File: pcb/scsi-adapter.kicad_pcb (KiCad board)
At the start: 4 copper layers, 120 x 90 mm, 406 parts, among them J101 Bench 5V, J201 TERMPWR jumper, J301 IDC50 box header, J302 HD50 female R/A, J303 2x17 box header, J401 TC2030-IDC, J501 TF PUSH, J601 USB-C (HRO TYPE-C-31-M-12), Q1001 FDV301N, Q1101 FDV301N, Q1201 FDV301N, Q1301 FDV301N, Q1401 FDV301N, Q1501 FDV301N, Q1601 FDV301N, Q1701 FDV301N, Q1801 FDV301N, Q1901 FDV301N, Q2001 FDV301N, Q201 2N7002, Q2101 FDV301N, Q2301 FDV301N, Q901 FDV301N, SW301 DIP 2-pos, SW401 BOOTSEL, SW402 RUN, U1001 74LVC1G17GW, U101 TPS259470ARPWR, U102 TPS2116DRLR, U103 TPS73701DCQR, U104 TPS73701DCQR, U1101 74LVC1G17GW, U1201 74LVC1G17GW, U1301 74LVC1G17GW, U1401 74LVC1G17GW, U1501 74LVC1G17GW, U1601 74LVC1G17GW, U1701 74LVC1G17GW, U1801 74LVC1G17GW, U1901 74LVC1G17GW, U2001 74LVC1G17GW, U201 TPS259470ARPWR, U202 LM393DR2G, U203 CJ431, U2101 74LVC1G17GW, U2201 74LVC1G17GW, U2301 74LVC1G17GW, U2401 74LVC1G17GW, U2501 74LVC1G17GW, U2601 74LVC1G17GW, U301 SN74LVTH245APWR, U302 SN74LVTH245APWR, U303 SN74LVTH245APWR, U401 RP2350B, U402 W25Q128JVSIQ, U403 APS6404L-3SQR-SN, U501 TCA9555PWR, U601 CH334P, U701 FT232HL, U702 93LC56BT-I/OT, U901 74LVC1G17GW, Y401 12MHz ABM8-272-T3, Y601 12MHz ABM8-272-T3, Y701 12MHz ABM8-272-T3

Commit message: more manual iteration
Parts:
- moved C108 0.41 mm to (105.2, 87.0)
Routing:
- net GND: track 291.4 -> 297.9 mm, vias 193 -> 195
- net /BENCH_5V: track 23.3 -> 24.6 mm
- net /scsi/~{DB0}: track 164.9 -> 163.8 mm
- net /scsi/~{DB2}: track 166.5 -> 165.4 mm
- net /scsi/~{DB1}: track 165.3 -> 164.1 mm
- net /scsi/~{MSG}: track 86.4 -> 85.3 mm
- net /scsi/~{BSY}: track 101.4 -> 100.3 mm
- net /scsi/~{SEL}: track 89.7 -> 88.6 mm
- net /scsi/~{RST}: track 86.0 -> 84.9 mm
- net /scsi/~{IO}: track 74.1 -> 72.9 mm
- net /scsi/~{DBP}: track 144.2 -> 143.1 mm
- net /scsi/~{DB6}: track 143.9 -> 142.7 mm
- net /scsi/~{DB5}: track 155.3 -> 154.1 mm
- net /scsi/~{DB4}: track 154.4 -> 153.3 mm
- net /scsi/~{DB3}: track 154.5 -> 153.4 mm
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
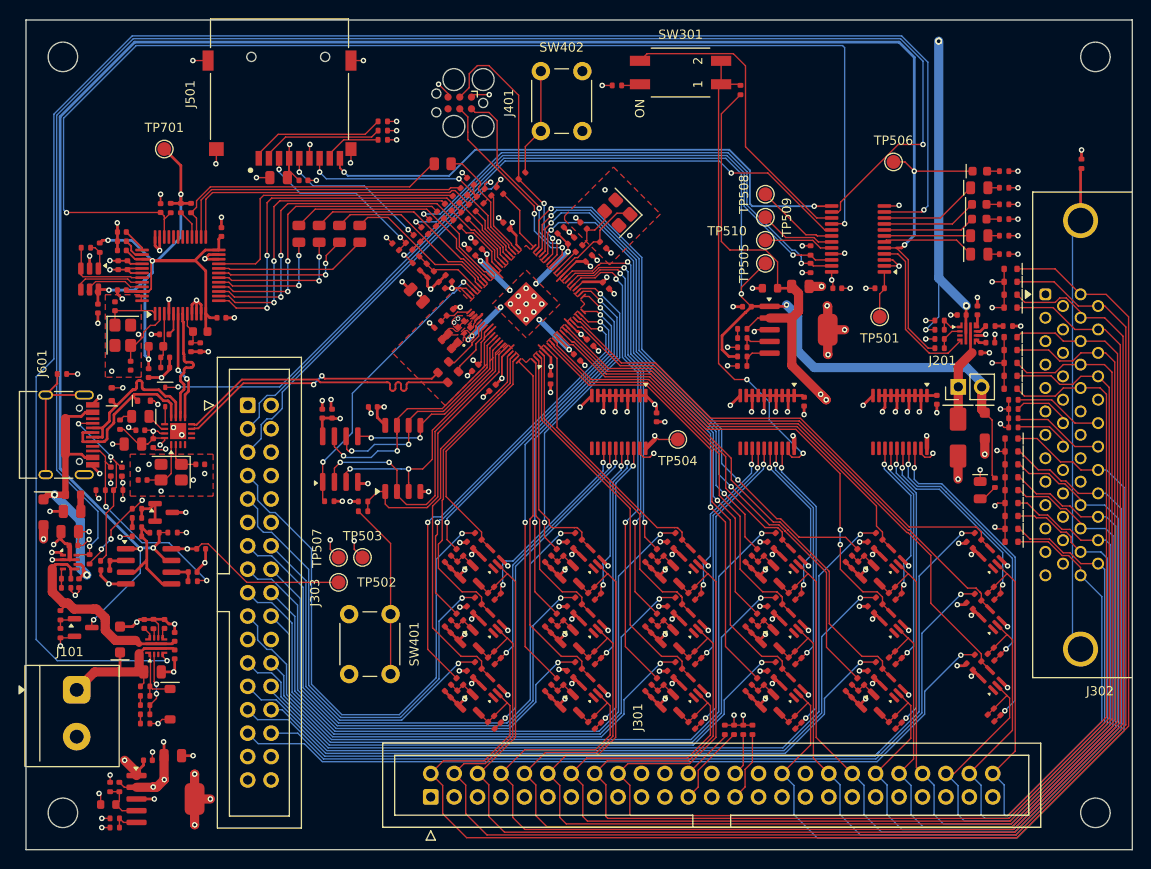
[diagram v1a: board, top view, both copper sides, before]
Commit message: thermal pours for LDOs
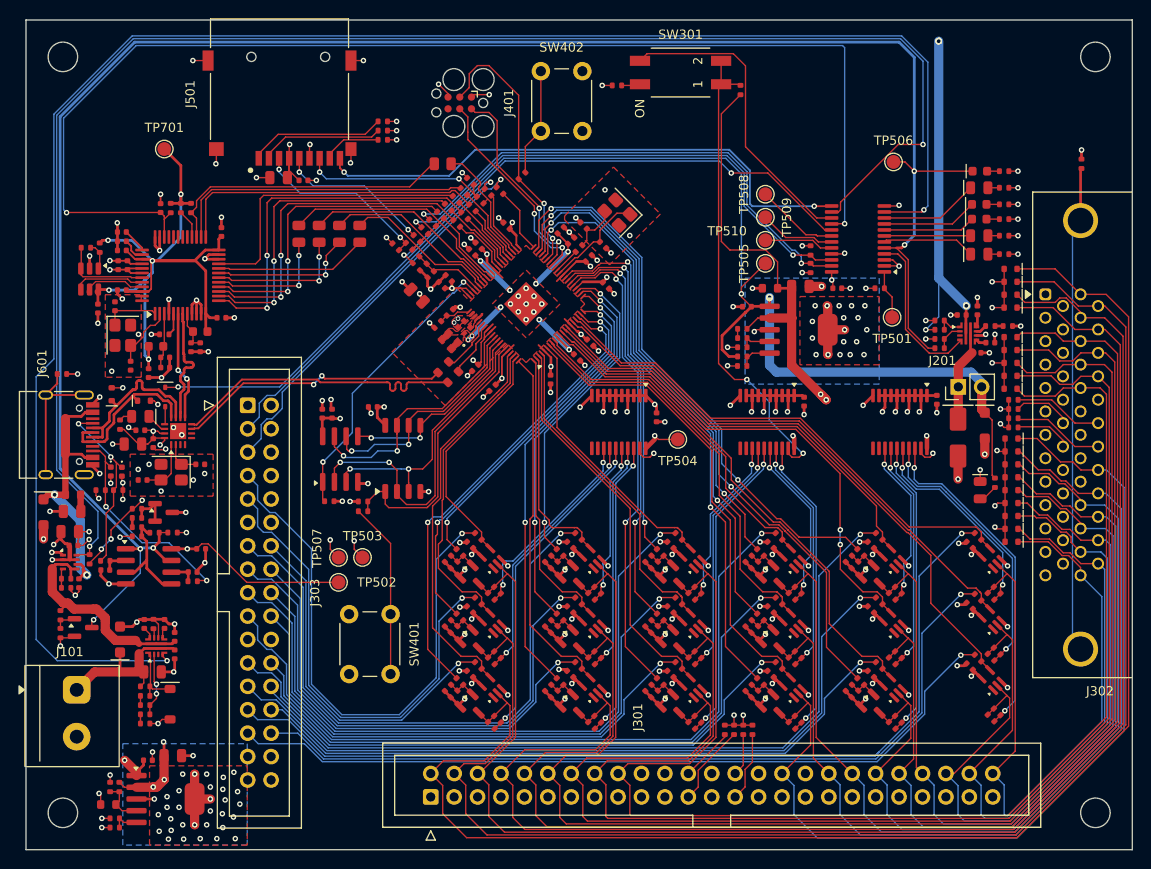
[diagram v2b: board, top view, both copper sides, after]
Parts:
- moved TP501 1.35 mm to (193.9, 62.2)
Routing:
- net TERMPWR: track 116.8 -> 120.2 mm
- net VTERMINATOR: track 95.3 -> 94.7 mm
- net GND: vias 195 -> 238
- added copper zone on B.Cu, net GND

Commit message: update docs
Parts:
- moved C712 2.05 mm to (112.4, 53.5), turned to 90 degrees
- moved C703 1.15 mm to (113.2, 67.2)
- moved C708 0.81 mm to (115.0, 66.9)
- moved FB701 0.74 mm to (114.5, 64.8)
- moved C709 0.66 mm to (115.0, 66.0)
- moved R701 0.55 mm to (115.0, 63.5)
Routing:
- net /ft232h/FT232H_VCCA: track 2.66 -> 1.10 mm
- net FT232H_3V3: track 79.2 -> 77.7 mm
- net GND: track 297.9 -> 296.5 mm, vias 238 -> 241
- net /ft232h/FT232H_REF: track 2.44 -> 1.89 mm
- net /ft232h/FT232H_VPHY: track 5.99 -> 5.46 mm
